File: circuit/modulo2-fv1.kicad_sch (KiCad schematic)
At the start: 67 parts, among them J1 CONN_01X04, J3 CONN_01X02, J4 HOLE, J5 HOLE, J6 USB_OTG, SW1 ROTENC_BOURNS_PEL12D, U1 NE5532, U10 TLE2426, U2 PWR_CONN, U3 FV-1, U4 AVR-ISP6, U5 LM1117 3V3, U6 ATmega328p, U7 DBG_UART, U8 74164, Y1 16MHz

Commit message: getting closer to the final PCBs; still have to change the rotenc
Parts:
- added C6: 1nF, myAmp:C_1206, symbol myAmp:C
- added R24: 10K, myAmp:R_10MM, symbol myAmp:R
- added R25: 1K, myAmp:R_10MM, symbol myAmp:R
- added U9: AMPCTRL, myAmp:PIN_1x03, symbol myAmp:AMPCTRL
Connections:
- net +24V: now also R24.1
- net GND: now also C6.1, R25.2, U9.1 (GND)
- net POW_MUTE: now reaches U6.2 ((XCK/T0)PD4)
- net POW_MUTE: now also U9.3 (MUTE)
- net IN_V: now reaches U6.22 (ADC7)
- net IN_V: now also C6.2, R24.2, R25.1
- net POW_RST: now reaches U6.30 ((RXD)PD0)
- net POW_RST: now also U9.2 (RESET)
- no-connect marks 12 -> 9

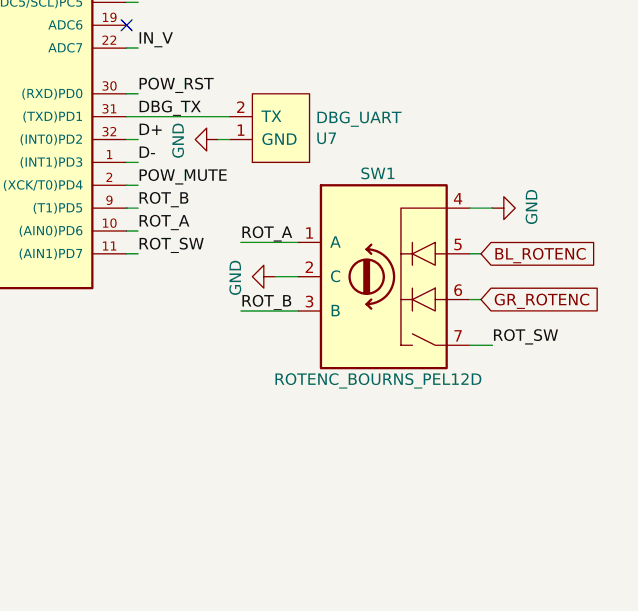
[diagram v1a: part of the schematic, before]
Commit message: usb has been changed to accommodate fab capabilities; moved the rotenc deeper into the board
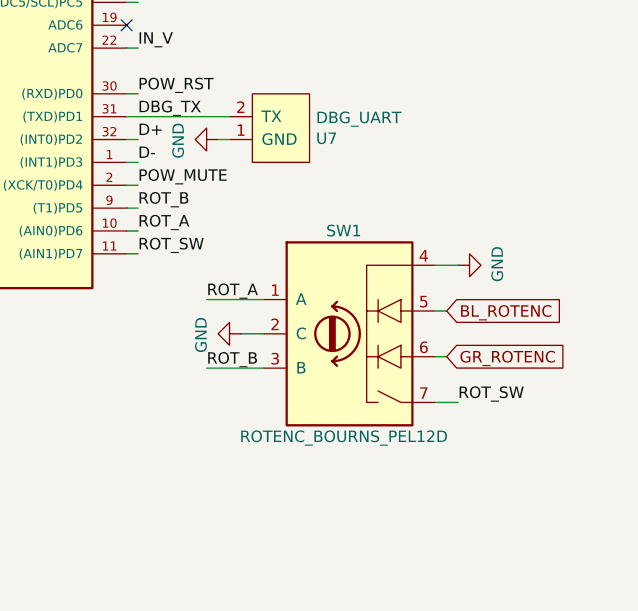
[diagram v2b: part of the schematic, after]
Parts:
- J6: footprint myAmp:USB_OTG_THT -> myAmp:USB_OTG_THT_simple
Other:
- moved on the sheet: SW1
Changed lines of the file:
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@@
     (stroke (width 0) (type default) (color 0 0 0 0))
   )
-  (wire (pts (xy 245.11 146.05) (xy 251.46 146.05))
+  (wire (pts (xy 241.3 152.4) (xy 247.65 152.4))
     (stroke (width 0) (type default) (color 0 0 0 0))
   )
@@
     (stroke (width 0) (type default) (color 0 0 0 0))
   )
-  (wire (pts (xy 270.51 134.62) (xy 273.05 134.62))
+  (wire (pts (xy 266.7 140.97) (xy 269.24 140.97))
     (stroke (width 0) (type default) (color 0 0 0 0))
   )
@@
     (stroke (width 0) (type default) (color 0 0 0 0))
   )
-  (wire (pts (xy 251.46 142.24) (xy 248.92 142.24))
+  (wire (pts (xy 247.65 148.59) (xy 245.11 148.59))
     (stroke (width 0) (type default) (color 0 0 0 0))
   )
@@
     (stroke (width 0) (type default) (color 0 0 0 0))
   )
-  (wire (pts (xy 270.51 144.78) (xy 271.78 144.78))
+  (wire (pts (xy 266.7 151.13) (xy 267.97 151.13))
     (stroke (width 0) (type default) (color 0 0 0 0))
   )
@@
     (stroke (width 0) (type default) (color 0 0 0 0))
   )
-  (wire (pts (xy 270.51 149.86) (xy 273.05 149.86))
+  (wire (pts (xy 266.7 156.21) (xy 269.24 156.21))
     (stroke (width 0) (type default) (color 0 0 0 0))
   )
@@
     (stroke (width 0) (type default) (color 0 0 0 0))
   )
-  (wire (pts (xy 270.51 139.7) (xy 271.78 139.7))
+  (wire (pts (xy 266.7 146.05) (xy 267.97 146.05))
     (stroke (width 0) (type default) (color 0 0 0 0))
   )
@@
     (stroke (width 0) (type default) (color 0 0 0 0))
   )
-  (wire (pts (xy 245.11 138.43) (xy 251.46 138.43))
+  (wire (pts (xy 241.3 144.78) (xy 247.65 144.78))
     (stroke (width 0) (type default) (color 0 0 0 0))
   )
@@
     (effects (font (size 1.27 1.27)) (justify left bottom))
   )
-  (label "ROT_SW" (at 273.05 149.86 0)
+  (label "ROT_SW" (at 269.24 156.21 0)
     (effects (font (size 1.27 1.27)) (justify left bottom))
   )
@@
     (effects (font (size 1.27 1.27)) (justify left bottom))
   )
-  (label "ROT_B" (at 245.11 146.05 0)
+  (label "ROT_B" (at 241.3 152.4 0)
     (effects (font (size 1.27 1.27)) (justify left bottom))
   )
@@
     (effects (font (size 1.27 1.27)) (justify left bottom))
   )
-  (label "ROT_A" (at 245.11 138.43 0)
+  (label "ROT_A" (at 241.3 144.78 0)
     (effects (font (size 1.27 1.27)) (justify left bottom))
   )
@@
     )
   )
-  (global_label "GR_ROTENC" (shape input) (at 271.78 144.78 0) (fields_autoplaced)
+  (global_label "GR_ROTENC" (shape input) (at 267.97 151.13 0) (fields_autoplaced)
     (effects (font (size 1.27 1.27)) (justify left))
-    (property "Intersheet References" "${INTERSHEET_REFS}" (id 0) (at 284.9294 144.7006 0)
+    (property "Intersheet References" "${INTERSHEET_REFS}" (id 0) (at 281.1194 151.0506 0)
       (effects (font (size 1.27 1.27)) (justify left) hide)
     )
@@
     )
   )
-  (global_label "BL_ROTENC" (shape input) (at 271.78 139.7 0) (fields_autoplaced)
+  (global_label "BL_ROTENC" (shape input) (at 267.97 146.05 0) (fields_autoplaced)
     (effects (font (size 1.27 1.27)) (justify left))
-    (property "Intersheet References" "${INTERSHEET_REFS}" (id 0) (at 284.6875 139.6206 0)
+    (property "Intersheet References" "${INTERSHEET_REFS}" (id 0) (at 280.8775 145.9706 0)
       (effects (font (size 1.27 1.27)) (justify left) hide)
     )
@@
     (pin "2")
   )
-  (symbol (lib_id "power:GND") (at 248.92 142.24 270) (unit 1)
+  (symbol (lib_id "power:GND") (at 245.11 148.59 270) (unit 1)
     (in_bom yes) (on_board yes)
-    (property "Reference" "#PWR024" (id 0) (at 242.57 142.24 0)
+    (property "Reference" "#PWR024" (id 0) (at 238.76 148.59 0)
       (effects (font (size 1.27 1.27)) hide)
     )
-    (property "Value" "GND" (id 1) (at 244.5258 142.367 0))
-    (property "Footprint" "" (id 2) (at 248.92 142.24 0)
+    (property "Value" "GND" (id 1) (at 240.7158 148.717 0))
+    (property "Footprint" "" (id 2) (at 245.11 148.59 0)
       (effects (font (size 1.27 1.27)) hide)
     )
-    (property "Datasheet" "" (id 3) (at 248.92 142.24 0)
+    (property "Datasheet" "" (id 3) (at 245.11 148.59 0)
       (effects (font (size 1.27 1.27)) hide)
     )
@@
     (pin "2")
   )
-  (symbol (lib_id "myAmp:ROTENC_BOURNS_PEL12D") (at 259.08 142.24 0) (unit 1)
+  (symbol (lib_id "myAmp:ROTENC_BOURNS_PEL12D") (at 255.27 148.59 0) (unit 1)
     (in_bom yes) (on_board yes)
-    (property "Reference" "SW1" (id 0) (at 260.35 130.81 0))
-    (property "Value" "ROTENC_BOURNS_PEL12D" (id 1) (at 260.35 153.67 0))
-    (property "Footprint" "myAmp:BOURNS_PEL12D-2xxx" (id 2) (at 256.54 138.176 0)
+    (property "Reference" "SW1" (id 0) (at 256.54 137.16 0))
+    (property "Value" "ROTENC_BOURNS_PEL12D" (id 1) (at 256.54 160.02 0))
+    (property "Footprint" "myAmp:BOURNS_PEL12D-2xxx" (id 2) (at 252.73 144.526 0)
       (effects (font (size 1.27 1.27)) hide)
     )
-    (property "Datasheet" "" (id 3) (at 259.08 135.636 0)
+    (property "Datasheet" "" (id 3) (at 255.27 141.986 0)
       (effects (font (size 1.27 1.27)) hide)
     )
@@
     (property "Reference" "J6" (id 0) (at 120.015 154.94 0))
     (property "Value" "USB_OTG" (id 1) (at 120.015 157.48 0))
-    (property "Footprint" "myAmp:USB_OTG_THT" (id 2) (at 124.46 168.91 0)
+    (property "Footprint" "myAmp:USB_OTG_THT_simple" (id 2) (at 124.46 168.91 0)
       (effects (font (size 1.27 1.27)) hide)
     )
@@
     (pin "2")
   )
-  (symbol (lib_id "power:GND") (at 273.05 134.62 90) (unit 1)
+  (symbol (lib_id "power:GND") (at 269.24 140.97 90) (unit 1)
     (in_bom yes) (on_board yes)
-    (property "Reference" "#PWR023" (id 0) (at 279.4 134.62 0)
+    (property "Reference" "#PWR023" (id 0) (at 275.59 140.97 0)
       (effects (font (size 1.27 1.27)) hide)
     )
-    (property "Value" "GND" (id 1) (at 277.4442 134.493 0))
-    (property "Footprint" "" (id 2) (at 273.05 134.62 0)
+    (property "Value" "GND" (id 1) (at 273.6342 140.843 0))
+    (property "Footprint" "" (id 2) (at 269.24 140.97 0)
       (effects (font (size 1.27 1.27)) hide)
     )
-    (property "Datasheet" "" (id 3) (at 273.05 134.62 0)
+    (property "Datasheet" "" (id 3) (at 269.24 140.97 0)
       (effects (font (size 1.27 1.27)) hide)
     )
@@
     )
     (path "/4699291b-5ea2-4f18-89a9-48e46658cc16"
-      (reference "J6") (unit 1) (value "USB_OTG") (footprint "myAmp:USB_OTG_THT")
+      (reference "J6") (unit 1) (value "USB_OTG") (footprint "myAmp:USB_OTG_THT_simple")
     )
     (path "/7adc75ea-edbb-4fd7-b830-305e27e6d9e1"

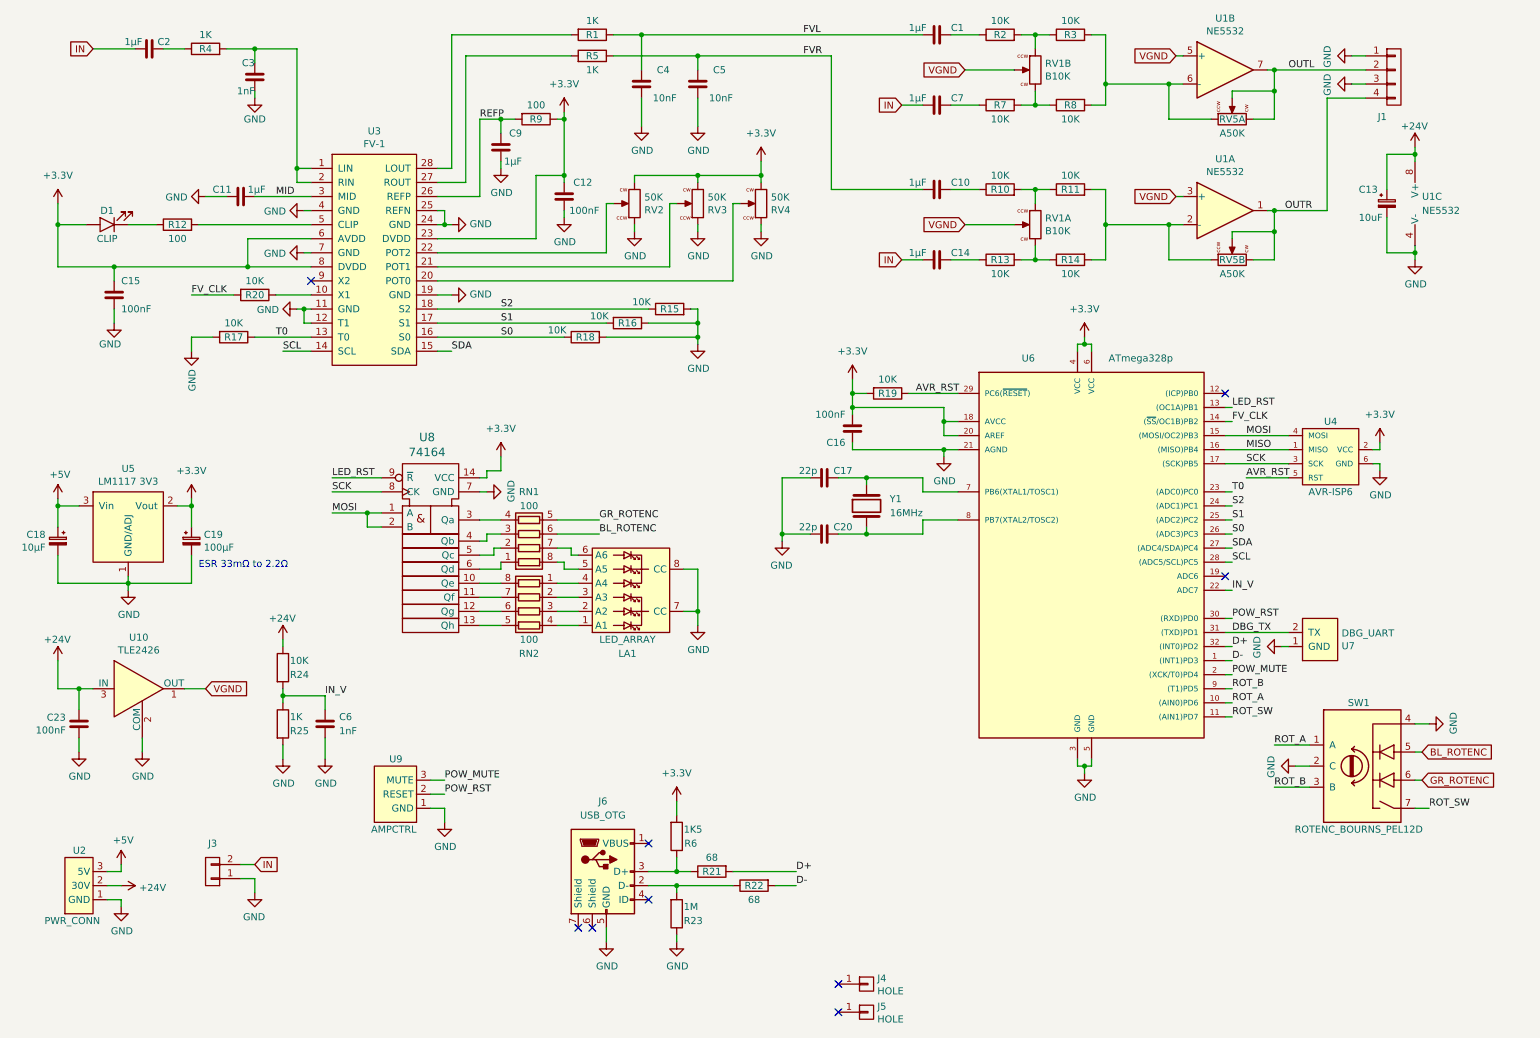
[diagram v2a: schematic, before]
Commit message: ditched the LED array board; LEDs are on the main PCB now
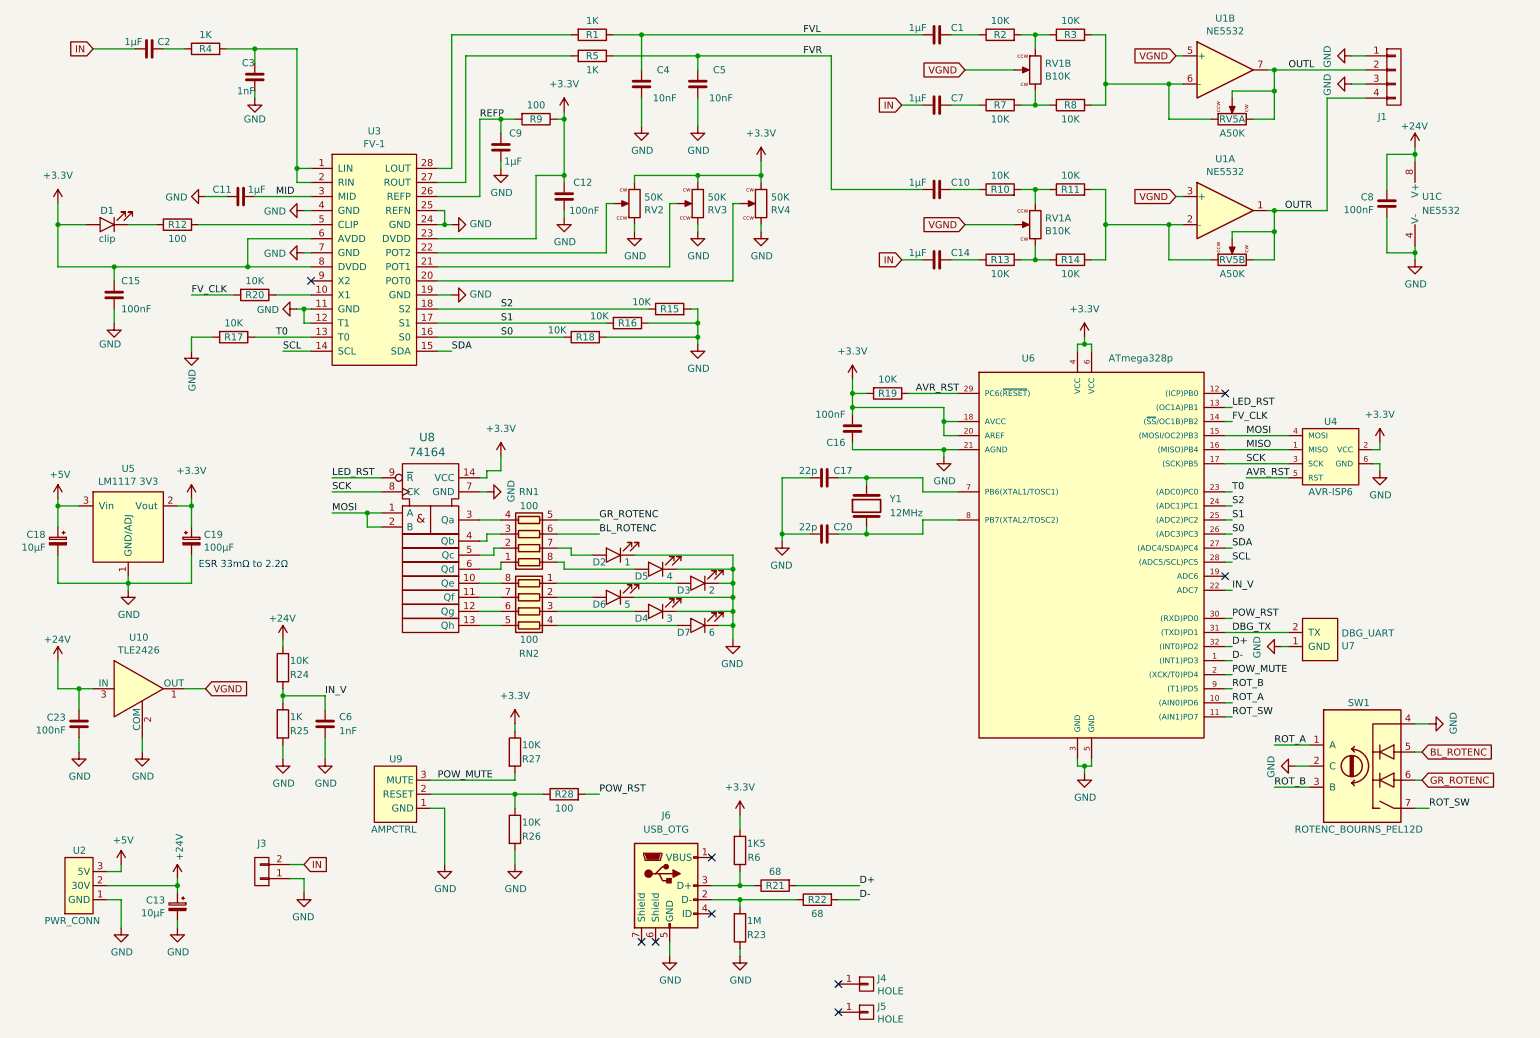
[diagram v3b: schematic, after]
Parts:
- removed LA1: LED_ARRAY, myAmp:LED_ARRAY, symbol myAmp:LED_ARRAY
- added C8: 100nF, myAmp:C_1206, symbol myAmp:C
- added D2: 1, myAmp:LED_D3.0mm_Horizontal_Long, symbol myAmp:LED
- added D3: 2, myAmp:LED_D3.0mm_Horizontal_Long, symbol myAmp:LED
- added D4: 3, myAmp:LED_D3.0mm_Horizontal_Long, symbol myAmp:LED
- added D5: 4, myAmp:LED_D3.0mm_Horizontal_Short, symbol myAmp:LED
- added D6: 5, myAmp:LED_D3.0mm_Horizontal_Short, symbol myAmp:LED
- added D7: 6, myAmp:LED_D3.0mm_Horizontal_Short, symbol myAmp:LED
- added R26, R27: 10K, myAmp:R_10MM, symbol myAmp:R
- added R28: 100, myAmp:R_10MM, symbol myAmp:R
- C13: value 10uF -> 10µF
- D1: value CLIP -> clip
- Y1: value 16MHz -> 12MHz
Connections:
- net +24V: now also C8.2
- net +3V3: now also R27.1
- net GND: now also C8.1, D2.1 (K), D3.1 (K), D4.1 (K), D5.1 (K), D6.1 (K), D7.1 (K), R26.2
- net POW_MUTE: now also R27.2
- net POW_RST: now also R28.2; no longer U9.2 (RESET)
- net at RN1.7 (R2.2): now also D2.2 (A)
- net at RN1.8 (R1.2): now also D5.2 (A)
- net at RN2.4 (R4.1): now also D7.2 (A)
- net at RN2.3 (R3.1): now also D4.2 (A)
- net at RN2.2 (R2.1): now also D6.2 (A)
- net at RN2.1 (R1.1): now also D3.2 (A)
- new net: R26.1, R28.1, U9.2 (RESET)
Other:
- moved on the sheet: J3, J6, R21, R22, R23, R6

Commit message: tweaked program selector LEDs
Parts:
- D1: footprint myAmp:LED_D3.0mm_PCBedge -> myAmp:LED_D3.0mm_Horizontal_Short
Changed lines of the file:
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@@
     (property "Reference" "D1" (id 0) (at 30.48 48.26 0))
     (property "Value" "clip" (id 1) (at 30.48 53.34 0))
-    (property "Footprint" "myAmp:LED_D3.0mm_PCBedge" (id 2) (at 30.48 50.8 0)
+    (property "Footprint" "myAmp:LED_D3.0mm_Horizontal_Short" (id 2) (at 30.48 50.8 0)
       (effects (font (size 1.27 1.27)) hide)
     )
@@
     )
     (path "/00000000-0000-0000-0000-00005ef2310d"
-      (reference "D1") (unit 1) (value "clip") (footprint "myAmp:LED_D3.0mm_PCBedge")
+      (reference "D1") (unit 1) (value "clip") (footprint "myAmp:LED_D3.0mm_Horizontal_Short")
     )
     (path "/f3e13532-3999-4d1f-800f-4b9a7b3c3e9d"

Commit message: almost there...
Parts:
- added T1: B0, myAmp:TestPin, symbol myAmp:TEST
- added T2: ADC6, myAmp:TestPin, symbol myAmp:TEST
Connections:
- net at U6.12 ((ICP)PB0): now also T1.1
- net at U6.19 (ADC6): now also T2.1
- no-connect marks 9 -> 7
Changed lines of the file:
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@@
   (no_connect (at 139.7 165.1))
   (no_connect (at 139.7 175.26))
-  (no_connect (at 232.41 81.28))
-  (no_connect (at 232.41 114.3))
   (no_connect (at 67.31 60.96))
   (wire (pts (xy 97.79 110.49) (xy 100.33 110.49))
@@
     (stroke (width 0) (type default) (color 0 0 0 0))
   )
+  (wire (pts (xy 232.41 114.3) (xy 237.49 114.3))
+    (stroke (width 0) (type default) (color 0 0 0 0))
+  )
   (wire (pts (xy 21.59 129.54) (xy 21.59 134.62))
     (stroke (width 0) (type default) (color 0 0 0 0))
@@
     (stroke (width 0) (type default) (color 0 0 0 0))
   )
+  (wire (pts (xy 232.41 81.28) (xy 242.57 81.28))
+    (stroke (width 0) (type default) (color 0 0 0 0))
+  )
   (wire (pts (xy 240.03 48.26) (xy 241.3 48.26))
     (stroke (width 0) (type default) (color 0 0 0 0))
@@
     (pin "1")
   )
+  (symbol (lib_id "myAmp:TEST") (at 245.11 81.28 0) (unit 1)
+    (in_bom yes) (on_board yes) (fields_autoplaced)
+    (property "Reference" "T1" (id 0) (at 246.38 80.0099 0)
+      (effects (font (size 1.27 1.27)) (justify left))
+    )
+    (property "Value" "B0" (id 1) (at 246.38 82.5499 0)
+      (effects (font (size 1.27 1.27)) (justify left))
+    )
+    (property "Footprint" "myAmp:TestPin" (id 2) (at 245.11 81.28 0)
+      (effects (font (size 1.27 1.27)) hide)
+    )
+    (property "Datasheet" "" (id 3) (at 245.11 81.28 0)
+      (effects (font (size 1.27 1.27)) hide)
+    )
+    (pin "1")
+  )
   (symbol (lib_id "myAmp:C") (at 69.85 140.97 180) (unit 1)
     (in_bom yes) (on_board yes)
@@
     (pin "2")
   )
+  (symbol (lib_id "myAmp:TEST") (at 240.03 114.3 0) (unit 1)
+    (in_bom yes) (on_board yes) (fields_autoplaced)
+    (property "Reference" "T2" (id 0) (at 241.3 113.0299 0)
+      (effects (font (size 1.27 1.27)) (justify left))
+    )
+    (property "Value" "ADC6" (id 1) (at 241.3 115.5699 0)
+      (effects (font (size 1.27 1.27)) (justify left))
+    )
+    (property "Footprint" "myAmp:TestPin" (id 2) (at 240.03 114.3 0)
+      (effects (font (size 1.27 1.27)) hide)
+    )
+    (property "Datasheet" "" (id 3) (at 240.03 114.3 0)
+      (effects (font (size 1.27 1.27)) hide)
+    )
+    (pin "1")
+  )
   (symbol (lib_id "myAmp:R_POT_DBL") (at 233.68 57.15 90) (unit 2)
     (in_bom yes) (on_board yes)
@@
       (reference "SW1") (unit 1) (value "ROTENC_BOURNS_PEL12D") (footprint "myAmp:BOURNS_PEL12D-2xxx")
     )
+    (path "/ad79abcb-9177-4ec3-958c-b80399bc5215"
+      (reference "T1") (unit 1) (value "B0") (footprint "myAmp:TestPin")
+    )
+    (path "/c8c3ba6e-6f6e-4a97-b351-bbff9b9bdcc2"
+      (reference "T2") (unit 1) (value "ADC6") (footprint "myAmp:TestPin")
+    )
     (path "/c63e1f50-3466-402f-b4f3-04e169a49b85"

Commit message: sent to fab!
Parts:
- J6: footprint myAmp:USB_OTG_THT_simple -> myAmp:USB_OTG_THT
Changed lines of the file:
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@@
     (property "Reference" "J6" (id 0) (at 131.445 157.48 0))
     (property "Value" "USB_OTG" (id 1) (at 131.445 160.02 0))
-    (property "Footprint" "myAmp:USB_OTG_THT_simple" (id 2) (at 135.89 171.45 0)
+    (property "Footprint" "myAmp:USB_OTG_THT" (id 2) (at 135.89 171.45 0)
       (effects (font (size 1.27 1.27)) hide)
     )
@@
     )
     (path "/4699291b-5ea2-4f18-89a9-48e46658cc16"
-      (reference "J6") (unit 1) (value "USB_OTG") (footprint "myAmp:USB_OTG_THT_simple")
+      (reference "J6") (unit 1) (value "USB_OTG") (footprint "myAmp:USB_OTG_THT")
     )
     (path "/00000000-0000-0000-0000-00005ef23215"
